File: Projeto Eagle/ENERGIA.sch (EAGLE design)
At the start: 10 parts, among them IC1 LM1117 5V, J1 CONECTOR, J2 MICRO-USB, J3 DCJ0202, U1 74HC132

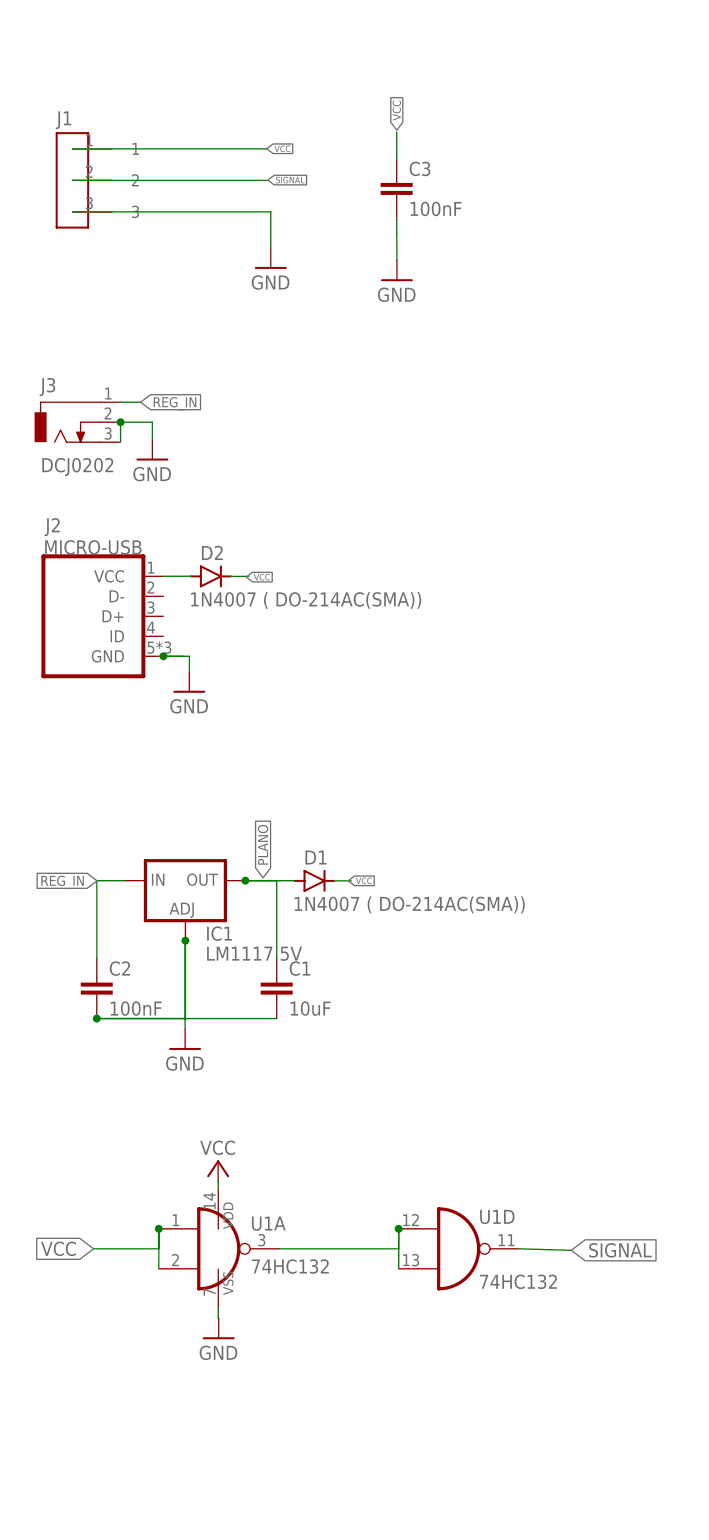
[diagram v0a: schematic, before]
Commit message: adição de nova entrada USB
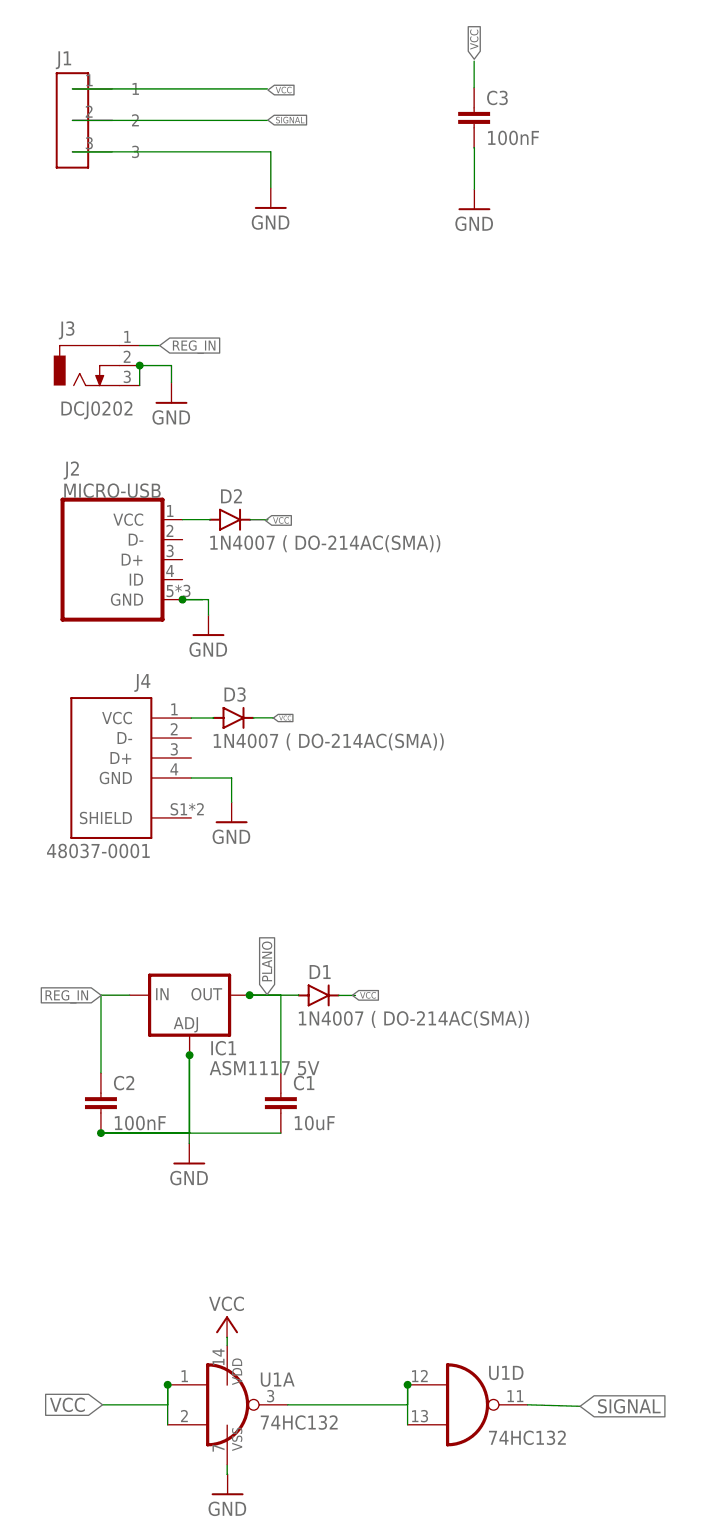
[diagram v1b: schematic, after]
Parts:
- added D3: 1N4007 ( DO-214AC(SMA)), diode:GF1
- added J4: 48037-0001, USB:48037-0001
- IC1: value LM1117 5V -> ASM1117 5V
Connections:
- new net N$4: D3.A, J4.VCC
- net GND: now also J4.GND
- net VCC: now also D3.C
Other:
- moved on the sheet: C1, C2, C3, D1, D2, IC1, J1, J2, J3, U1A, U1D

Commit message: adição de label para versionamento, correção de posição de vias e adição de plano GND no TOP layer
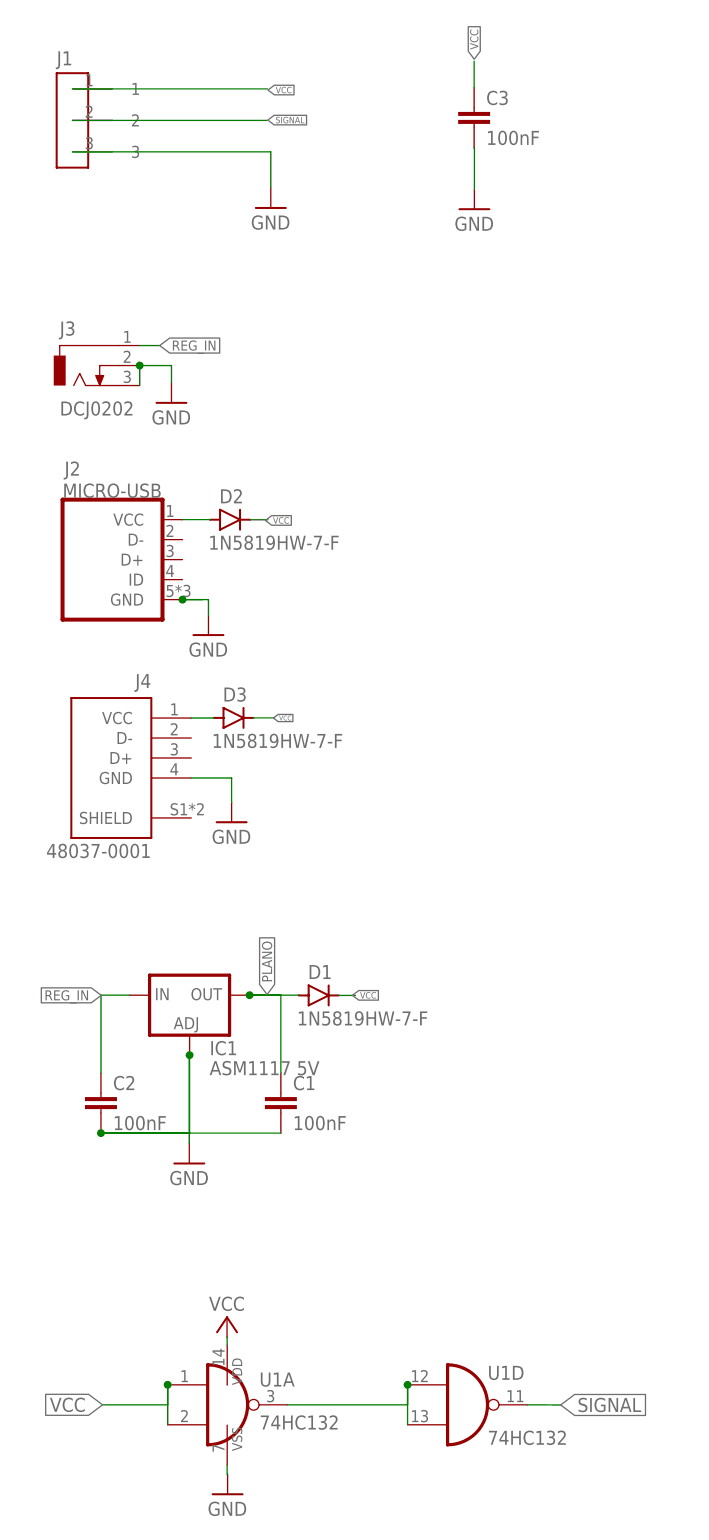
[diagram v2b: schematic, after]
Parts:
- C1: value 10uF -> 100nF
- D1, D2, D3: value 1N4007 ( DO-214AC(SMA)) -> 1N5819HW-7-F
- J1: value CONECTOR -> CONECTOR_FEMEA; device Eletroblocks Lib:CONECTOR -> Eletroblocks Lib:CONECTOR_FEMEA
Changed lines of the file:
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@@
 <parts>
 <part name="GND6" library="supply1" library_urn="urn:adsk.eagle:library:371" deviceset="GND" device=""/>
-<part name="J1" library="Eletroblocks Lib" deviceset="CONECTOR" device="" override_package3d_urn="urn:adsk.eagle:package:23099747/2" override_package_urn="urn:adsk.eagle:footprint:23099749/1"/>
+<part name="J1" library="Eletroblocks Lib" deviceset="CONECTOR_FEMEA" device="" override_package3d_urn="urn:adsk.eagle:package:23099747/2" override_package_urn="urn:adsk.eagle:footprint:23099749/1" override_locally_modified="yes"/>
 <part name="J3" library="con-jack" library_urn="urn:adsk.eagle:library:154" deviceset="DCJ0202" device="" package3d_urn="urn:adsk.eagle:package:7491/1" override_package3d_urn="urn:adsk.eagle:package:23099774/2" override_package_urn="urn:adsk.eagle:footprint:7486/1"/>
 <part name="J2" library="microusb" deviceset="MICRO-USB" device="" override_package3d_urn="urn:adsk.eagle:package:23099786/2" override_package_urn="urn:adsk.eagle:footprint:23099787/1"/>
 <part name="IC1" library="v-reg" library_urn="urn:adsk.eagle:library:409" deviceset="LD117A?*" device="S" package3d_urn="urn:adsk.eagle:package:30370/1" technology="18TR" value="ASM1117 5V"/>
 <part name="C2" library="rcl" library_urn="urn:adsk.eagle:library:334" deviceset="C-EU" device="C0805" package3d_urn="urn:adsk.eagle:package:23617/2" value="100nF"/>
-<part name="C1" library="rcl" library_urn="urn:adsk.eagle:library:334" deviceset="C-EU" device="C0805" package3d_urn="urn:adsk.eagle:package:23617/2" value="10uF"/>
+<part name="C1" library="rcl" library_urn="urn:adsk.eagle:library:334" deviceset="C-EU" device="C0805" package3d_urn="urn:adsk.eagle:package:23617/2" value="100nF"/>
 <part name="GND1" library="supply1" library_urn="urn:adsk.eagle:library:371" deviceset="GND" device=""/>
 <part name="GND2" library="supply1" library_urn="urn:adsk.eagle:library:371" deviceset="GND" device=""/>
 <part name="GND3" library="supply1" library_urn="urn:adsk.eagle:library:371" deviceset="GND" device=""/>
-<part name="D1" library="diode" library_urn="urn:adsk.eagle:library:210" deviceset="GF1" device="" package3d_urn="urn:adsk.eagle:package:43452/2" value="1N4007 ( DO-214AC(SMA))"/>
-<part name="D2" library="diode" library_urn="urn:adsk.eagle:library:210" deviceset="GF1" device="" package3d_urn="urn:adsk.eagle:package:43452/2" value="1N4007 ( DO-214AC(SMA))"/>
+<part name="D1" library="diode" library_urn="urn:adsk.eagle:library:210" deviceset="GF1" device="" package3d_urn="urn:adsk.eagle:package:43452/2" value="1N5819HW-7-F"/>
+<part name="D2" library="diode" library_urn="urn:adsk.eagle:library:210" deviceset="GF1" device="" package3d_urn="urn:adsk.eagle:package:43452/2" value="1N5819HW-7-F"/>
 <part name="J4" library="USB" deviceset="48037-0001" device="" override_package3d_urn="urn:adsk.eagle:package:23099797/2" override_package_urn="urn:adsk.eagle:footprint:23099798/1"/>
 <part name="GND4" library="supply1" library_urn="urn:adsk.eagle:library:371" deviceset="GND" device=""/>
-<part name="D3" library="diode" library_urn="urn:adsk.eagle:library:210" deviceset="GF1" device="" package3d_urn="urn:adsk.eagle:package:43452/2" value="1N4007 ( DO-214AC(SMA))"/>
+<part name="D3" library="diode" library_urn="urn:adsk.eagle:library:210" deviceset="GF1" device="" package3d_urn="urn:adsk.eagle:package:43452/2" value="1N5819HW-7-F"/>
 <part name="U1" library="40xx" library_urn="urn:adsk.eagle:library:80" deviceset="4011" device="D" package3d_urn="urn:adsk.eagle:package:823/2" value="74HC132"/>
 <part name="P+5" library="supply1" library_urn="urn:adsk.eagle:library:371" deviceset="VCC" device=""/>
@@
 <segment>
 <pinref part="U1" gate="D" pin="O"/>
-<wire x1="40.55" y1="-5.49" x2="47.23" y2="-5.68" width="0.1524" layer="91" grouprefs="SIGNAL"/>
-<label x="47.23" y="-5.68" size="1.778" layer="95" xref="yes" grouprefs="SIGNAL"/>
+<wire x1="40.55" y1="-5.49" x2="44.76" y2="-5.51" width="0.1524" layer="91" grouprefs="SIGNAL"/>
+<label x="44.76" y="-5.51" size="1.778" layer="95" xref="yes" grouprefs="SIGNAL"/>
 </segment>
 </net>
